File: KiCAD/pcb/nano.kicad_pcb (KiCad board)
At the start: 2 copper layers, 69.8 x 49.5 mm, 24 parts, among them J1 Barrel_Jack_Switch, J2 Conn_01x02_Male, J3 Conn_01x02_Male, J4 Conn_01x04_Male, J5 Conn_01x03_Male, K1 SANYOU_SRD_Form_C, K2 SANYOU_SRD_Form_C, P1 Digital, P2 Analog, Q1 S8050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

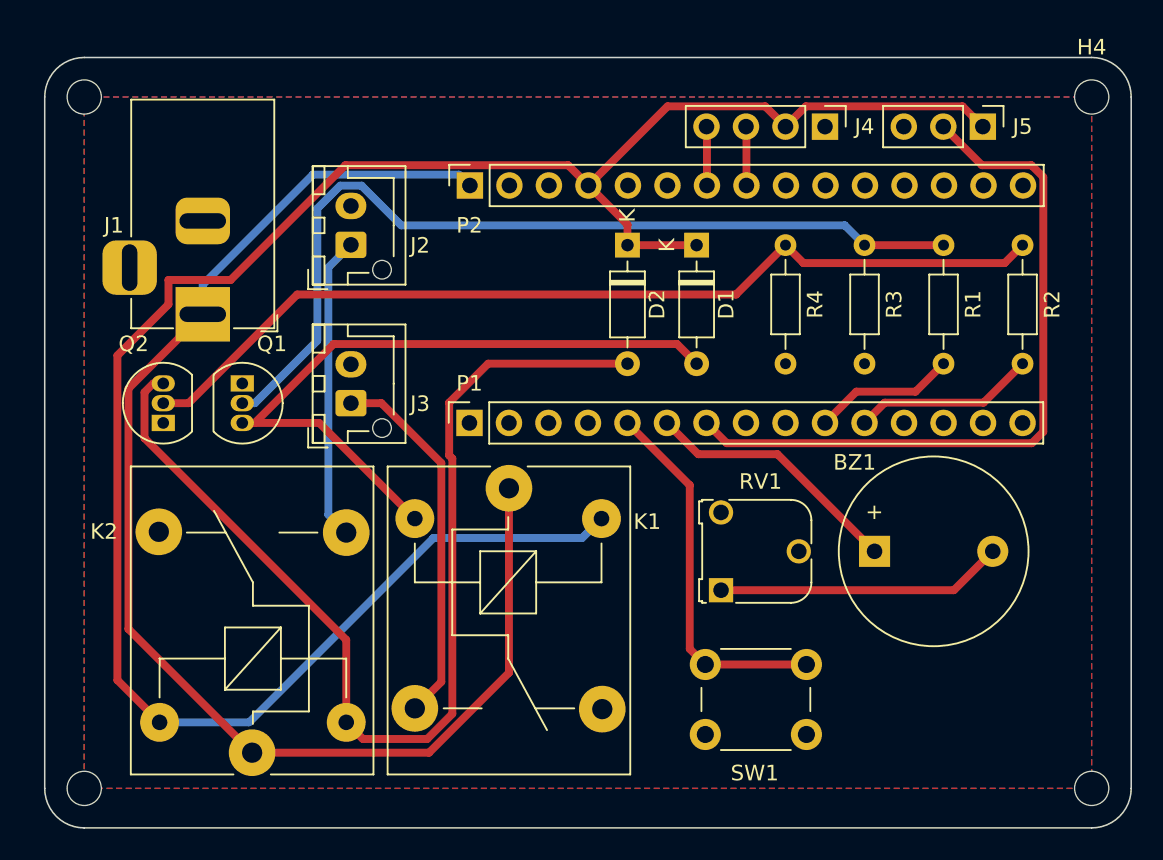
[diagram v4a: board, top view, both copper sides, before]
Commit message: added capacitor to fan
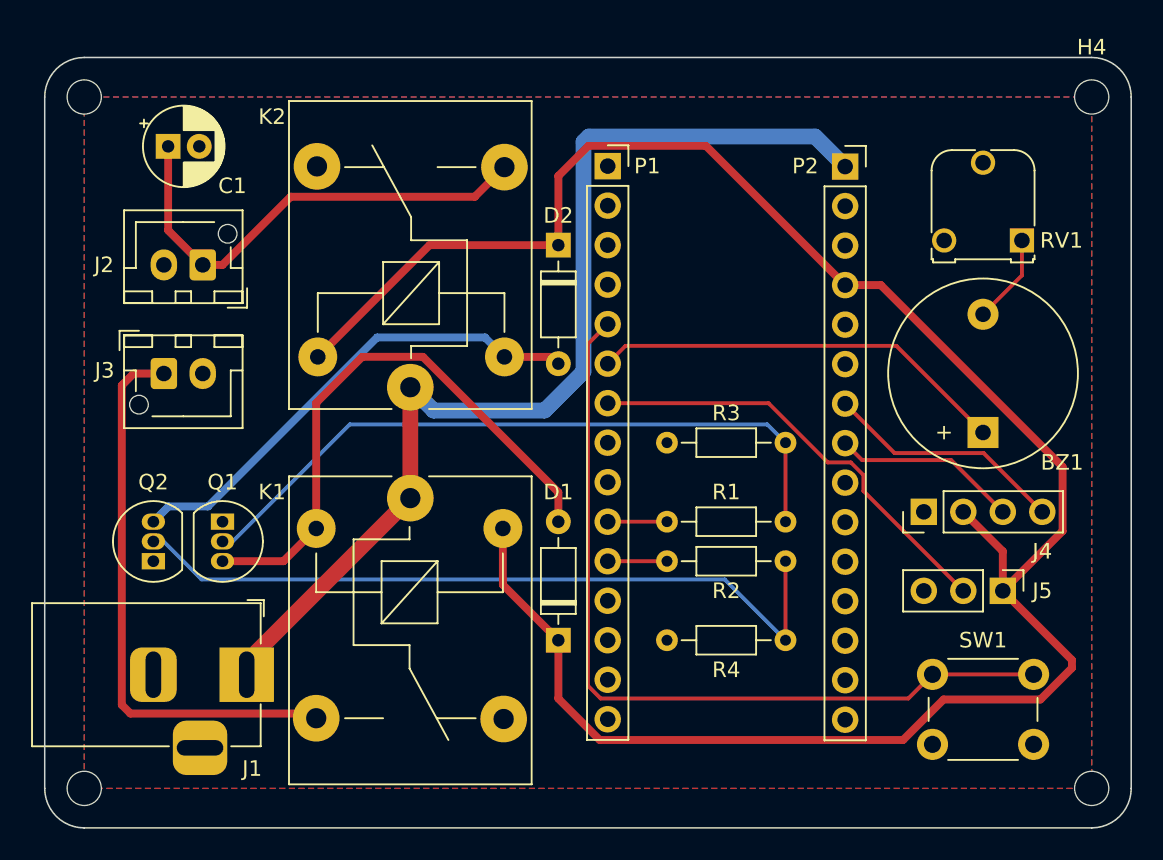
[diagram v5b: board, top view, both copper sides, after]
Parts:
- added C1: 10uF, Capacitor_THT:CP_Radial_D5.0mm_P2.00mm, F.Cu at (128.6, 97.8)
- moved J5 29.9 mm to (182.2, 126.4)
- moved RV1 29.7 mm to (183.5, 103.8), turned to 180 degrees
- moved D1 26.9 mm to (153.7, 129.5), turned to 90 degrees
- moved R2 26.2 mm to (160.7, 124.5), turned to 0 degrees
- moved K2 25.6 mm to (144.2, 113.3)
- moved J4 25.6 mm to (177.2, 121.3), turned to 90 degrees
- moved P2 24.2 mm to (172.1, 99.1), turned to 0 degrees
- moved J1 23.3 mm to (133.6, 131.8), turned to 0 degrees
- moved R1 20.5 mm to (160.7, 121.9), turned to 0 degrees
- moved R4 19.3 mm to (160.7, 129.5), turned to 0 degrees
- moved P1 18.8 mm to (156.8, 99.1), turned to 0 degrees
- moved SW1 14.6 mm to (177.7, 131.7)
- moved R3 13.7 mm to (160.7, 116.8), turned to 0 degrees
- moved J3 12.2 mm to (128.3, 112.4), turned to 0 degrees
- moved BZ1 10.3 mm to (181.0, 116.2), turned to 90 degrees
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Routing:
- net Net-(D2-Pad2): track 68.6 -> 31.6 mm
- net CTRL: track 24.1 -> 53.4 mm
- net DHT11: track 46.6 -> 28.5 mm
- net +12V: track 86.3 -> 68.2 mm
- net Net-(BZ1-Pad2): track 18.5 -> 5.78 mm
- net Net-(Q1-Pad2): track 57.4 -> 44.9 mm
- net HEATER_VCC: track 23.9 -> 36.4 mm
- net Net-(Q2-Pad2): track 60.4 -> 48.4 mm
- net LCD_I2C_SCL: track 3.80 -> 15.6 mm
- net FAN_VCC: track 19.6 -> 30.5 mm
- net BUZZER: track 16.8 -> 26.9 mm
- net Net-(D1-Pad2): track 45.5 -> 37.3 mm
- net ICD_I2C_SDA: track 3.80 -> 12.0 mm
- net FAN_RELAY: track 11.7 -> 3.81 mm
- net HEATER_RELAY: track 9.20 -> 3.81 mm
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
